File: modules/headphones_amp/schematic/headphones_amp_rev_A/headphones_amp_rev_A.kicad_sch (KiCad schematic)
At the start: 99 parts, among them J1 AudioJack3_SwitchTR, J2 AudioJack3_SwitchTR, J3 Conn_01x02, J4 Conn_01x02, Q1 BC140, Q10 BC548, Q11 BC548, Q12 BC140, Q13 BC160, Q14 BC548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

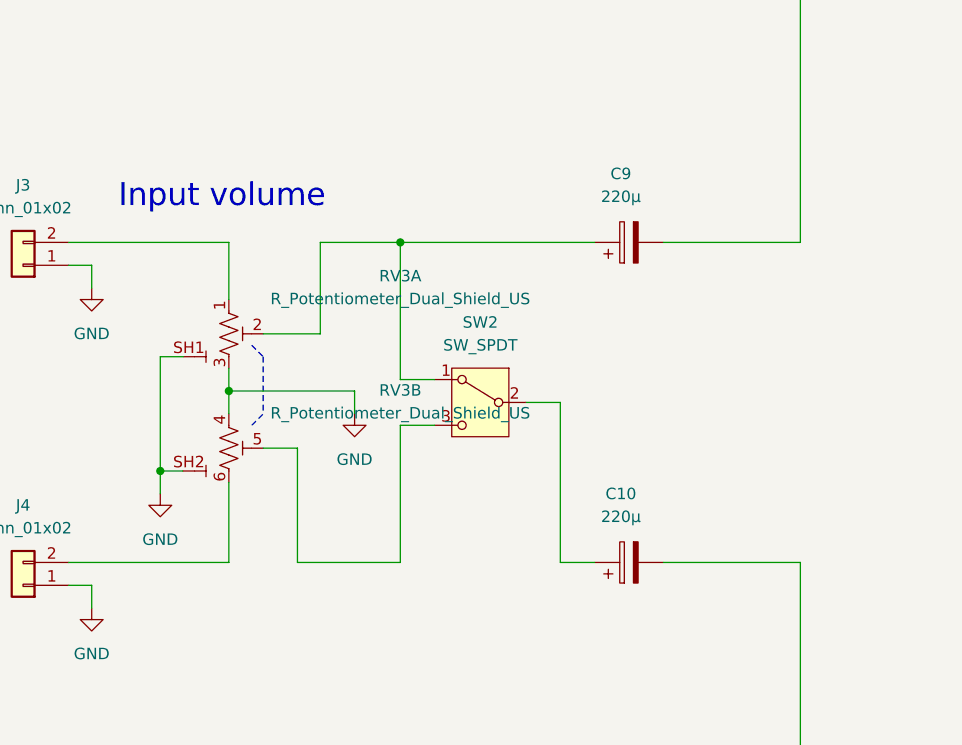
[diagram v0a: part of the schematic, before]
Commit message: fixed the footprint issue with the PTV
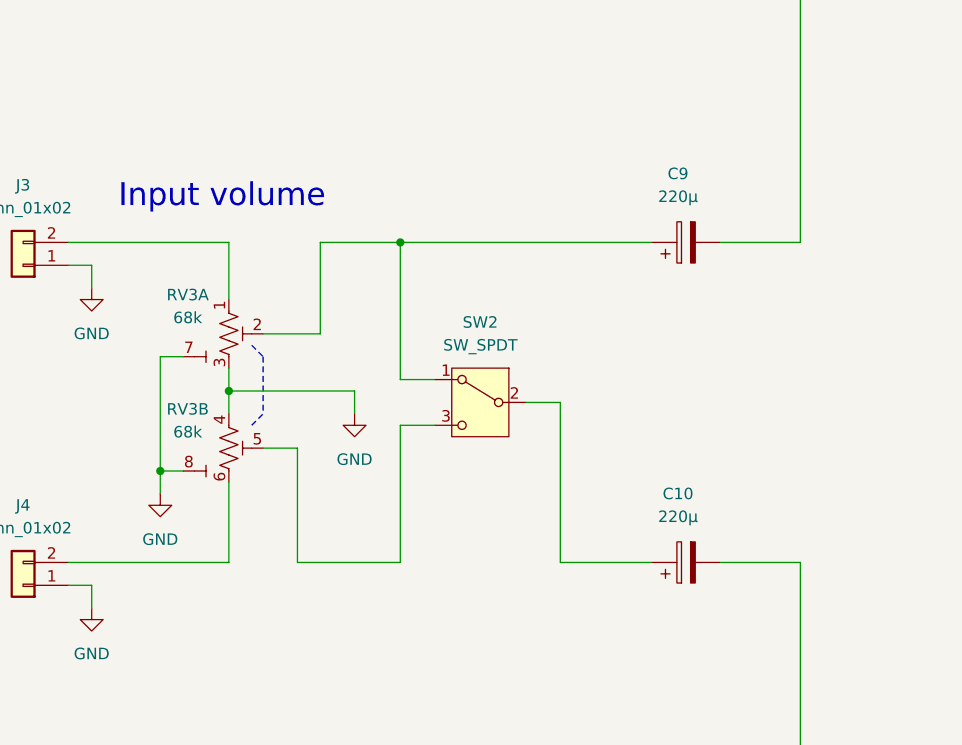
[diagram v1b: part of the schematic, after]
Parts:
- RV3: value R_Potentiometer_Dual_Shield_US -> 68k
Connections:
- net GND: now also RV3.7 (SH1), RV3.8 (SH2); no longer RV3.SH1 (Shield_1), RV3.SH2 (Shield_2)
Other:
- moved on the sheet: C10, C9
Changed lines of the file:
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@@
 	(wire
 		(pts
-			(xy 80.01 184.15) (xy 83.82 184.15)
+			(xy 80.01 184.15) (xy 90.17 184.15)
 		)
 		(stroke
@@
 	(wire
 		(pts
-			(xy 91.44 184.15) (xy 106.68 184.15)
+			(xy 97.79 184.15) (xy 106.68 184.15)
 		)
 		(stroke
@@
 	(wire
 		(pts
-			(xy 62.23 148.59) (xy 83.82 148.59)
+			(xy 62.23 148.59) (xy 90.17 148.59)
 		)
 		(stroke
@@
 	(wire
 		(pts
-			(xy 91.44 148.59) (xy 106.68 148.59)
+			(xy 97.79 148.59) (xy 106.68 148.59)
 		)
 		(stroke
@@
 	)
 	(symbol
-		(lib_id "ProjectLib_Transient:R_Potentiometer_Dual_Shield_US")
-		(at 43.18 158.75 0)
-		(unit 1)
-		(exclude_from_sim no)
-		(in_bom yes)
-		(on_board yes)
-		(dnp no)
-		(fields_autoplaced yes)
-		(property "Reference" "RV3"
-			(at 62.23 152.3298 0)
-			(effects
-				(font
-					(size 1.27 1.27)
-				)
-			)
-		)
-		(property "Value" "R_Potentiometer_Dual_Shield_US"
-			(at 62.23 154.8698 0)
-			(effects
-				(font
-					(size 1.27 1.27)
-				)
-			)
-		)
-		(property "Footprint" "ProjectLib_Transient:Potentiometer_Bourns_PTV112-4_Dual_Vertical"
-			(at 43.434 177.8 0)
-			(effects
-				(font
-					(size 1.27 1.27)
-				)
-				(hide yes)
-			)
-		)
-		(property "Datasheet" "~"
-			(at 43.18 158.75 0)
-			(effects
-				(font
-					(size 1.27 1.27)
-				)
-				(hide yes)
-			)
-		)
-		(property "Description" "Dual potentiometer (US symbol) with shield connection"
-			(at 49.784 145.542 0)
-			(effects
-				(font
-					(size 1.27 1.27)
-				)
-				(hide yes)
-			)
-		)
-		(pin "SH1"
-		)
-		(pin "5"
-		)
-		(pin "SH2"
-		)
-		(pin "4"
-		)
-		(pin "6"
-		)
-		(pin "3"
-		)
-		(pin "1"
-		)
-		(pin "2"
-		)
-		(instances
-			(project ""
-				(path "/d2365754-669a-45b0-8c88-535b259ec7b7"
-					(reference "RV3")
-					(unit 1)
-				)
-			)
-		)
-	)
-	(symbol
 		(lib_id "power:GND")
 		(at 57.15 167.64 0)
@@
 	)
 	(symbol
-		(lib_id "ProjectLib_Transient:R_Potentiometer_Dual_Shield_US")
-		(at 43.18 171.45 0)
-		(unit 2)
-		(exclude_from_sim no)
-		(in_bom yes)
-		(on_board yes)
-		(dnp no)
-		(fields_autoplaced yes)
-		(property "Reference" "RV3"
-			(at 62.23 165.0298 0)
-			(effects
-				(font
-					(size 1.27 1.27)
-				)
-			)
-		)
-		(property "Value" "R_Potentiometer_Dual_Shield_US"
-			(at 62.23 167.5698 0)
-			(effects
-				(font
-					(size 1.27 1.27)
-				)
-			)
-		)
-		(property "Footprint" "ProjectLib_Transient:Potentiometer_Bourns_PTV112-4_Dual_Vertical"
-			(at 43.434 190.5 0)
-			(effects
-				(font
-					(size 1.27 1.27)
-				)
-				(hide yes)
-			)
-		)
-		(property "Datasheet" "~"
-			(at 43.18 171.45 0)
-			(effects
-				(font
-					(size 1.27 1.27)
-				)
-				(hide yes)
-			)
-		)
-		(property "Description" "Dual potentiometer (US symbol) with shield connection"
-			(at 49.784 158.242 0)
-			(effects
-				(font
-					(size 1.27 1.27)
-				)
-				(hide yes)
-			)
-		)
-		(pin "SH1"
-		)
-		(pin "5"
-		)
-		(pin "SH2"
-		)
-		(pin "4"
-		)
-		(pin "6"
-		)
-		(pin "3"
-		)
-		(pin "1"
-		)
-		(pin "2"
-		)
-		(instances
-			(project ""
-				(path "/d2365754-669a-45b0-8c88-535b259ec7b7"
-					(reference "RV3")
-					(unit 2)
-				)
-			)
-		)
-	)
-	(symbol
 		(lib_id "Device:R_US")
 		(at 120.65 234.95 0)
@@
 	)
 	(symbol
+		(lib_id "ProjectLib_Transient:R_Potentiometer_Dual_Shield_US")
+		(at 43.18 158.75 0)
+		(unit 1)
+		(exclude_from_sim no)
+		(in_bom yes)
+		(on_board yes)
+		(dnp no)
+		(property "Reference" "RV3"
+			(at 38.608 154.432 0)
+			(effects
+				(font
+					(size 1.27 1.27)
+				)
+			)
+		)
+		(property "Value" "68k"
+			(at 38.608 156.972 0)
+			(effects
+				(font
+					(size 1.27 1.27)
+				)
+			)
+		)
+		(property "Footprint" "ProjectLib_Transient:Potentiometer_Bourns_PTV112-4_Dual_Vertical"
+			(at 43.434 177.8 0)
+			(effects
+				(font
+					(size 1.27 1.27)
+				)
+				(hide yes)
+			)
+		)
+		(property "Datasheet" "~"
+			(at 43.18 158.75 0)
+			(effects
+				(font
+					(size 1.27 1.27)
+				)
+				(hide yes)
+			)
+		)
+		(property "Description" "Dual potentiometer (US symbol) with shield connection"
+			(at 49.784 145.542 0)
+			(effects
+				(font
+					(size 1.27 1.27)
+				)
+				(hide yes)
+			)
+		)
+		(pin "1"
+		)
+		(pin "2"
+		)
+		(pin "3"
+		)
+		(pin "7"
+		)
+		(pin "8"
+		)
+		(pin "5"
+		)
+		(pin "6"
+		)
+		(pin "4"
+		)
+		(instances
+			(project ""
+				(path "/d2365754-669a-45b0-8c88-535b259ec7b7"
+					(reference "RV3")
+					(unit 1)
+				)
+			)
+		)
+	)
+	(symbol
 		(lib_id "Device:R_US")
 		(at 134.62 88.9 0)
@@
 	(symbol
 		(lib_id "Device:C_Polarized")
-		(at 87.63 184.15 90)
+		(at 93.98 184.15 90)
 		(unit 1)
 		(exclude_from_sim no)
@@
 		(fields_autoplaced yes)
 		(property "Reference" "C10"
-			(at 86.741 176.53 90)
+			(at 93.091 176.53 90)
 			(effects
 				(font
@@
 		)
 		(property "Value" "220µ"
-			(at 86.741 179.07 90)
+			(at 93.091 179.07 90)
 			(effects
 				(font
@@
 		)
 		(property "Footprint" "Capacitor_THT:CP_Radial_D10.0mm_P5.00mm"
-			(at 91.44 183.1848 0)
+			(at 97.79 183.1848 0)
 			(effects
 				(font
@@
 		)
 		(property "Datasheet" "~"
-			(at 87.63 184.15 0)
+			(at 93.98 184.15 0)
 			(effects
 				(font
@@
 		)
 		(property "Description" "Polarized capacitor"
-			(at 87.63 184.15 0)
+			(at 93.98 184.15 0)
 			(effects
 				(font
@@
 	(symbol
 		(lib_id "Device:C_Polarized")
-		(at 87.63 148.59 90)
+		(at 93.98 148.59 90)
 		(unit 1)
 		(exclude_from_sim no)
@@
 		(fields_autoplaced yes)
 		(property "Reference" "C9"
-			(at 86.741 140.97 90)
+			(at 93.091 140.97 90)
 			(effects
 				(font
@@
 		)
 		(property "Value" "220µ"
-			(at 86.741 143.51 90)
+			(at 93.091 143.51 90)
 			(effects
 				(font
@@
 		)
 		(property "Footprint" "Capacitor_THT:CP_Radial_D10.0mm_P5.00mm"
-			(at 91.44 147.6248 0)
+			(at 97.79 147.6248 0)
 			(effects
 				(font
@@
 		)
 		(property "Datasheet" "~"
-			(at 87.63 148.59 0)
+			(at 93.98 148.59 0)
 			(effects
 				(font
@@
 		)
 		(property "Description" "Polarized capacitor"
-			(at 87.63 148.59 0)
+			(at 93.98 148.59 0)
 			(effects
 				(font
@@
 				)
 			)
+		)
+	)
+	(symbol
+		(lib_id "ProjectLib_Transient:R_Potentiometer_Dual_Shield_US")
+		(at 43.18 171.45 0)
+		(unit 2)
+		(exclude_from_sim no)
+		(in_bom yes)
+		(on_board yes)
+		(dnp no)
+		(property "Reference" "RV3"
+			(at 38.608 167.132 0)
+			(effects
+				(font
+					(size 1.27 1.27)
+				)
+			)
+		)
+		(property "Value" "68k"
+			(at 38.608 169.672 0)
+			(effects
+				(font
+					(size 1.27 1.27)
+				)
+			)
+		)
+		(property "Footprint" "ProjectLib_Transient:Potentiometer_Bourns_PTV112-4_Dual_Vertical"
+			(at 43.434 190.5 0)
+			(effects
+				(font
+					(size 1.27 1.27)
+				)
+				(hide yes)
+			)
+		)
+		(property "Datasheet" "~"
+			(at 43.18 171.45 0)
+			(effects
+				(font
+					(size 1.27 1.27)
+				)
+				(hide yes)
+			)
+		)
+		(property "Description" "Dual potentiometer (US symbol) with shield connection"
+			(at 49.784 158.242 0)
+			(effects
+				(font
+					(size 1.27 1.27)
+				)
+				(hide yes)
+			)
+		)
+		(pin "1"
+		)
+		(pin "2"
+		)
+		(pin "3"
+		)
+		(pin "7"
+		)
+		(pin "8"
+		)
+		(pin "5"
+		)
+		(pin "6"
+		)
+		(pin "4"
+		)
+		(instances
+			(project ""
+				(path "/d2365754-669a-45b0-8c88-535b259ec7b7"
+					(reference "RV3")
+					(unit 2)
+				)
+			)

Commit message: added datasheets
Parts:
- removed R36, R4: 22, Resistor_THT:R_Axial_DIN0207_L6.3mm_D2.5mm_P10.16mm_Horizontal, symbol Device:R_US
- added RV4, RV7: 50, Potentiometer_THT:Potentiometer_Bourns_3296W_Vertical, symbol Device:R_Potentiometer_US
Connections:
- net GND: now also RV4.3, RV7.3
- net at C12.2, Q2.3 (C): now also RV4.1; no longer R6.1
- net at C14.2, Q13.3 (C): now also RV7.1; no longer R37.1
- new net: R37.1, RV7.2
- new net: R6.1, RV4.2

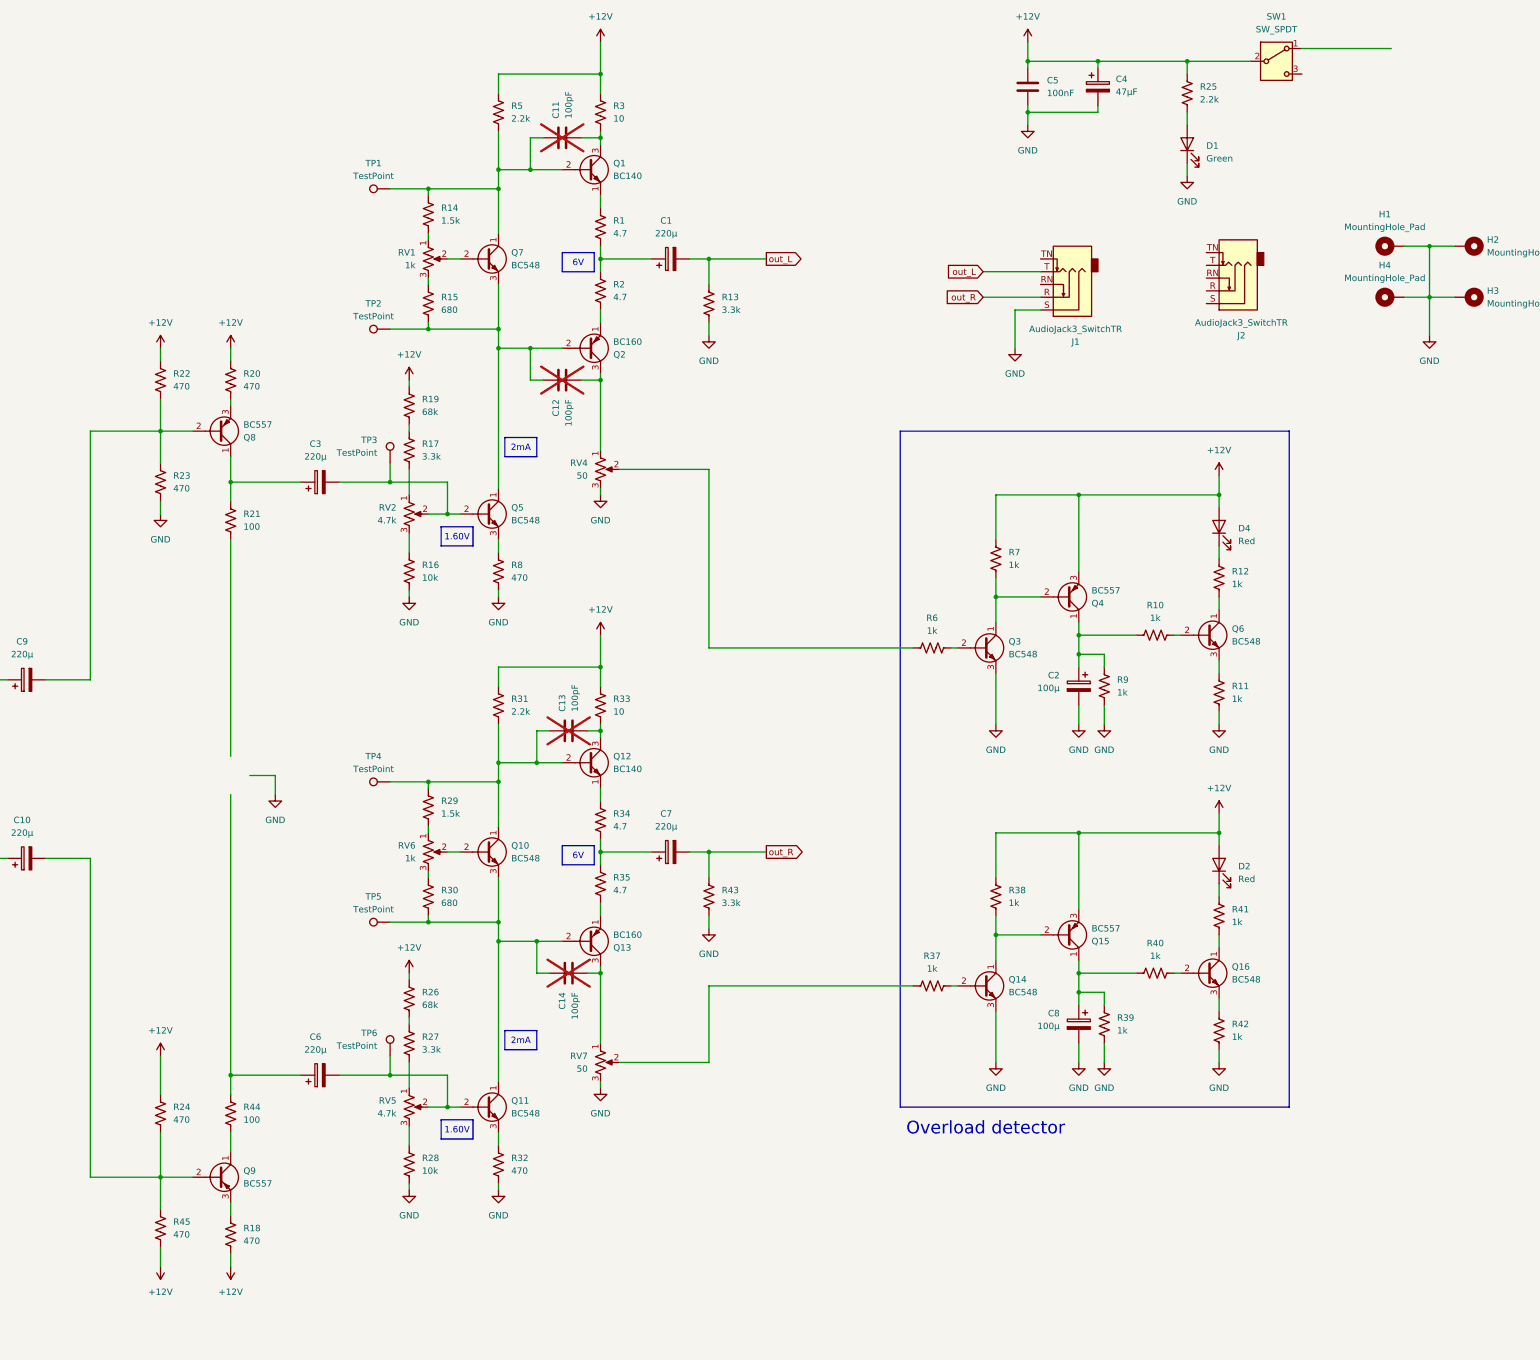
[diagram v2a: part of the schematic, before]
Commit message: added footprint for the 5.08mm board connector
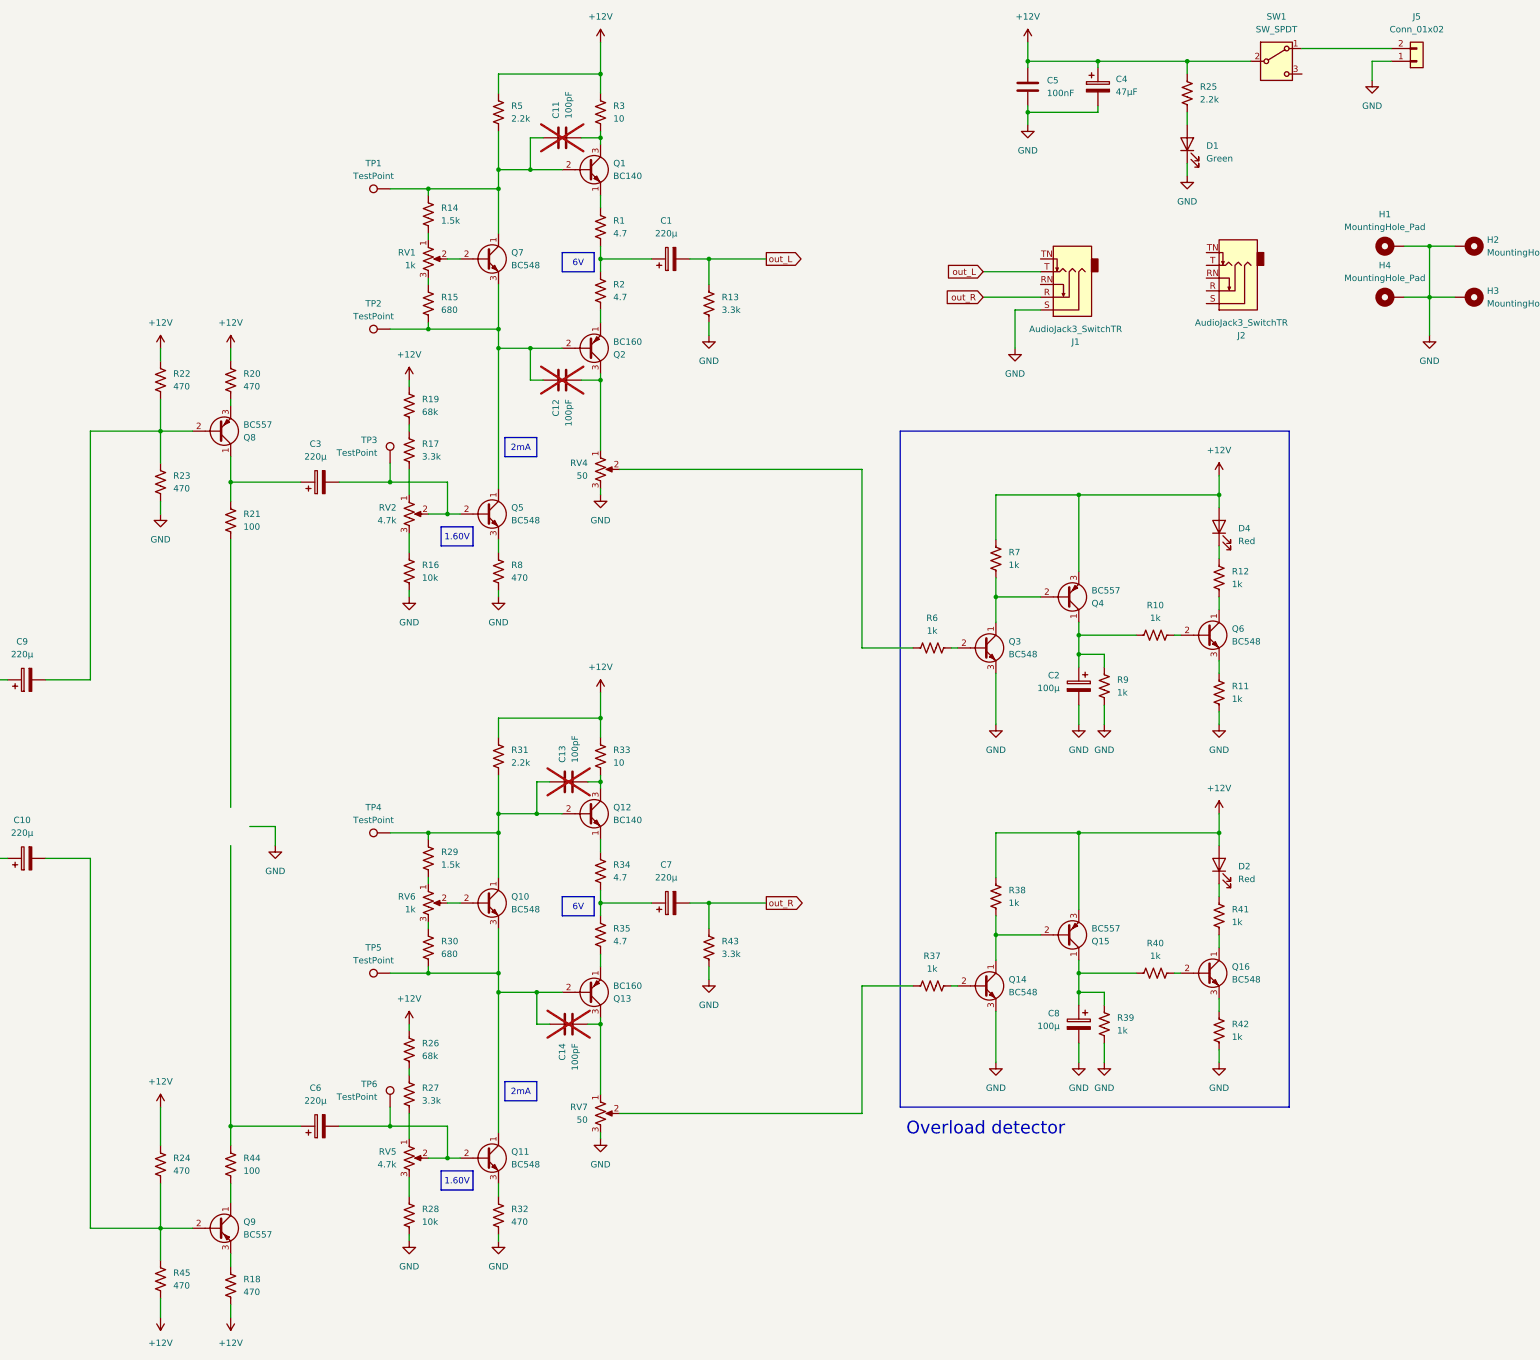
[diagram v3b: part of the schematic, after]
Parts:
- added J5: Conn_01x02, ProjectLib_Transient:WuerthElectronik_WR_TBL_Series_2545_1x02_P5.08mm_Horizontal, symbol Connector_Generic:Conn_01x02
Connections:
- net GND: now also J5.1 (Pin_1)
- net at SW1.1: now also J5.2 (Pin_2)
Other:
- moved on the sheet: C13, C14, C6, C7, Q10, Q11, Q12, Q13, Q9, R18, R24, R26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
